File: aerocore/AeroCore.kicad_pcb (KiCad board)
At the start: 2 copper layers, 60 x 60 mm, 50 parts, among them J1 USB_C_Receptacle_USB2.0_16P, J2 Conn_ARM_JTAG_SWD_10, J3 Conn_01x02_Pin, J4 Conn_01x06_Pin, Q1 DMG3418L, U1 RP2040, U2 AP2112K-3.3, U3 MCP73831-2-OT, U4 W25Q16JVUXIQ TR, U5 BMP388, Y2 12MHz

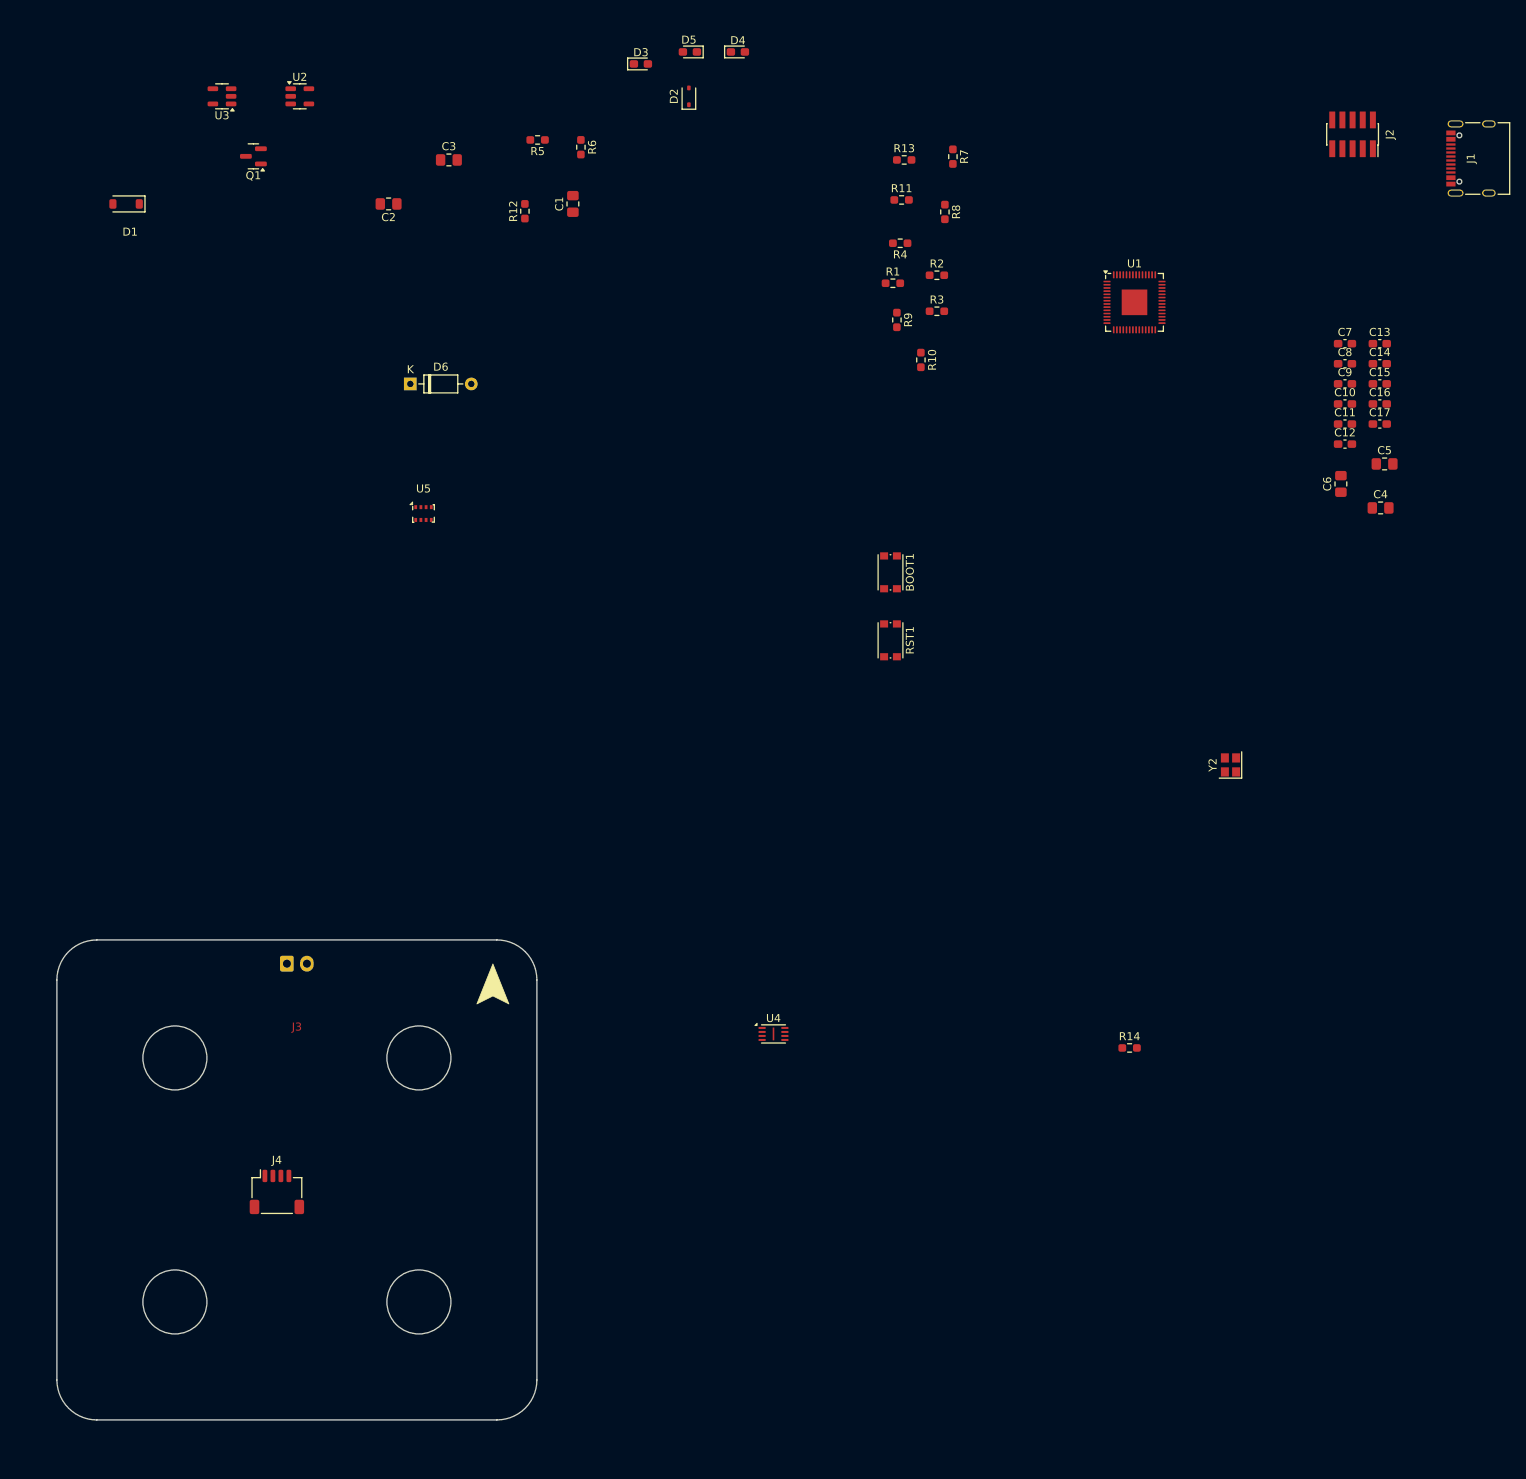
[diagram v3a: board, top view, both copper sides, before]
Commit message: update info for lis3mdltr
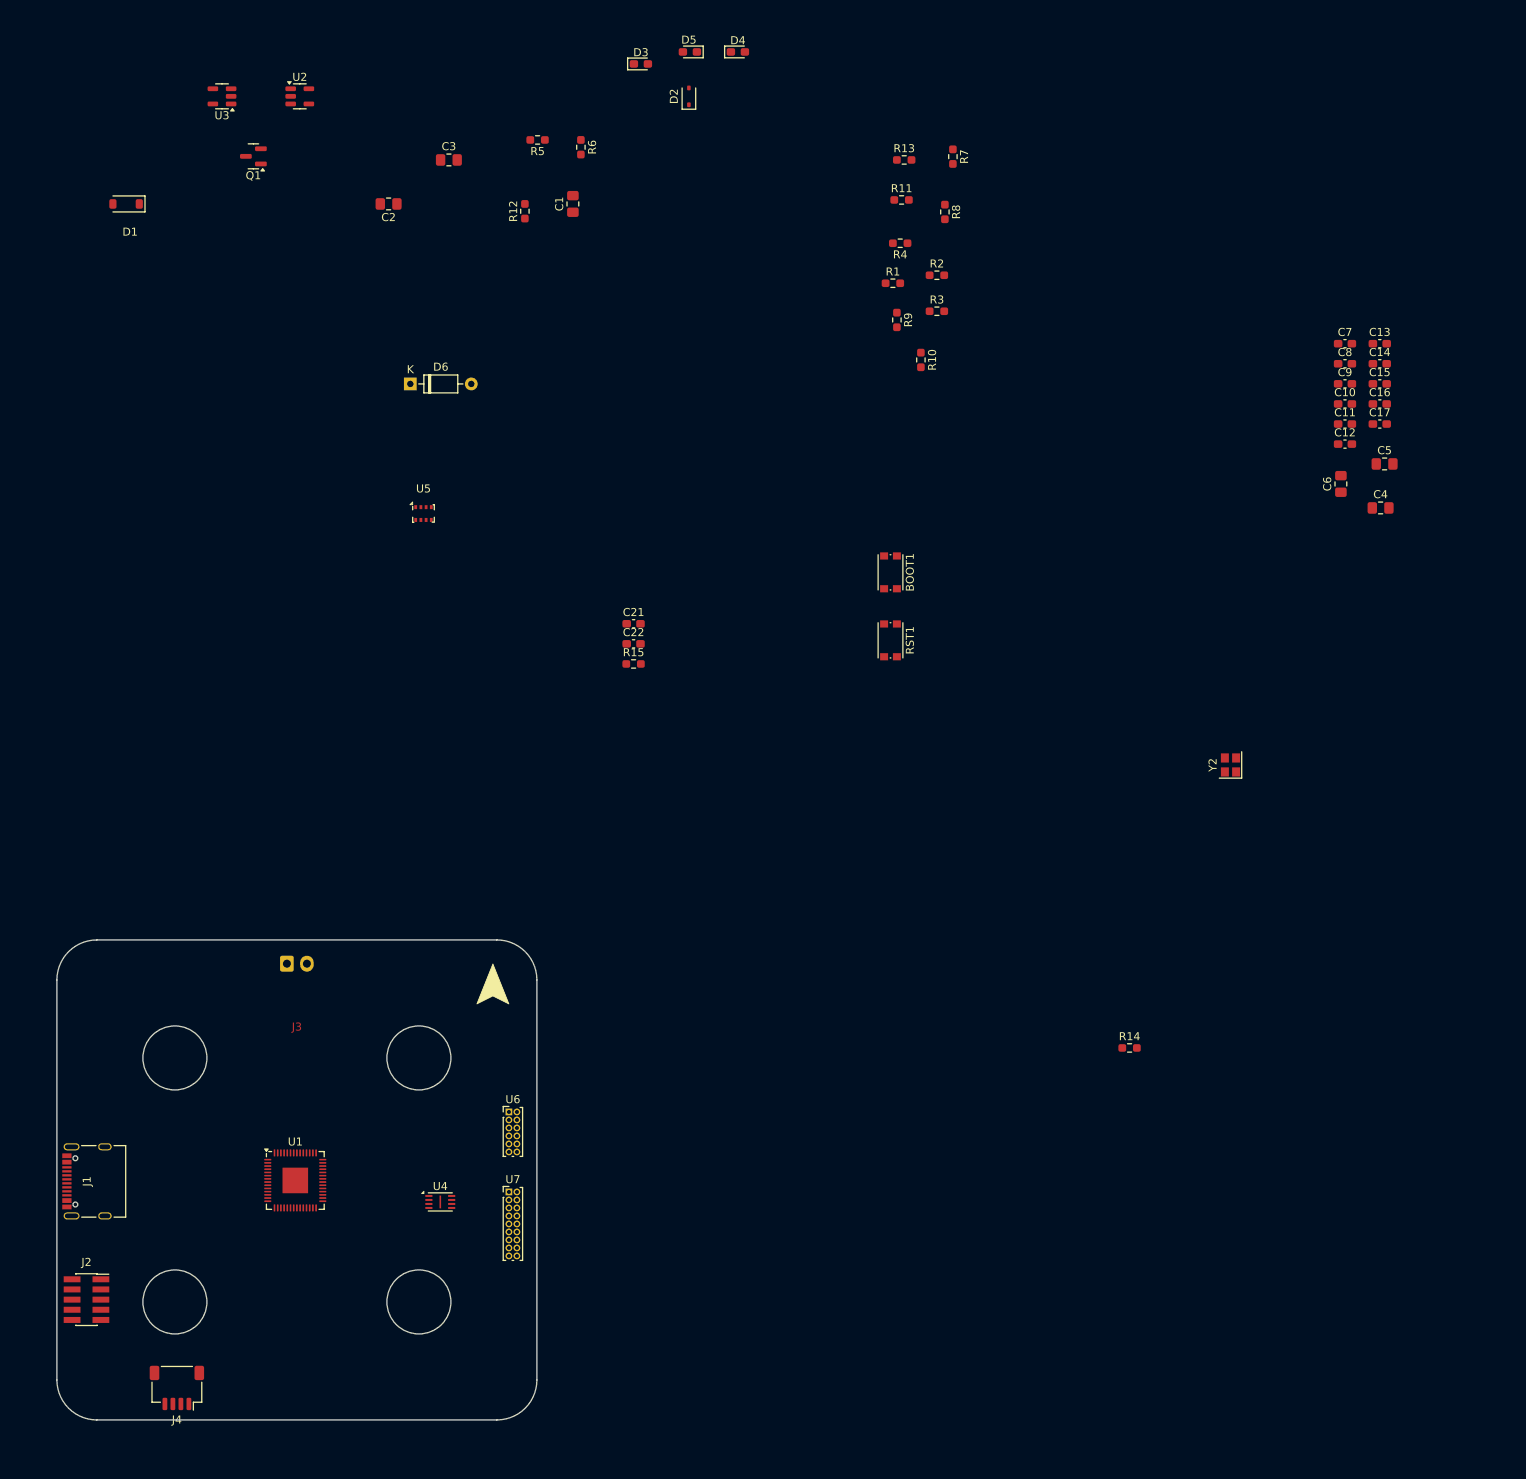
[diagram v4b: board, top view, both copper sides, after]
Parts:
- added C21: 0.1uF, Capacitor_SMD:C_0603_1608Metric_Pad1.08x0.95mm_HandSolder, F.Cu at (92.1, 90.5)
- added C22: 0.1uF, Capacitor_SMD:C_0603_1608Metric_Pad1.08x0.95mm_HandSolder, F.Cu at (92.1, 93.0)
- added R15: 10k, Resistor_SMD:R_0603_1608Metric_Pad0.98x0.95mm_HandSolder, F.Cu at (92.1, 95.5)
- added U6: LIS3MDL, Connector_PinHeader_1.00mm:PinHeader_2x06_P1.00mm_Vertical, F.Cu at (76.5, 151.5)
- added U7: ICM-20649, Connector_PinHeader_1.00mm:PinHeader_2x09_P1.00mm_Vertical, F.Cu at (76.5, 161.5)
- moved J1 215.1 mm to (23.8, 160.2)
- moved J2 215.1 mm to (23.7, 175.0), turned to 0 degrees
- moved U1 151.8 mm to (49.8, 160.1)
- moved U4 46.6 mm to (67.9, 162.8)
- moved J4 27.5 mm to (35.0, 186.0), turned to 180 degrees

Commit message: add pcb for old design
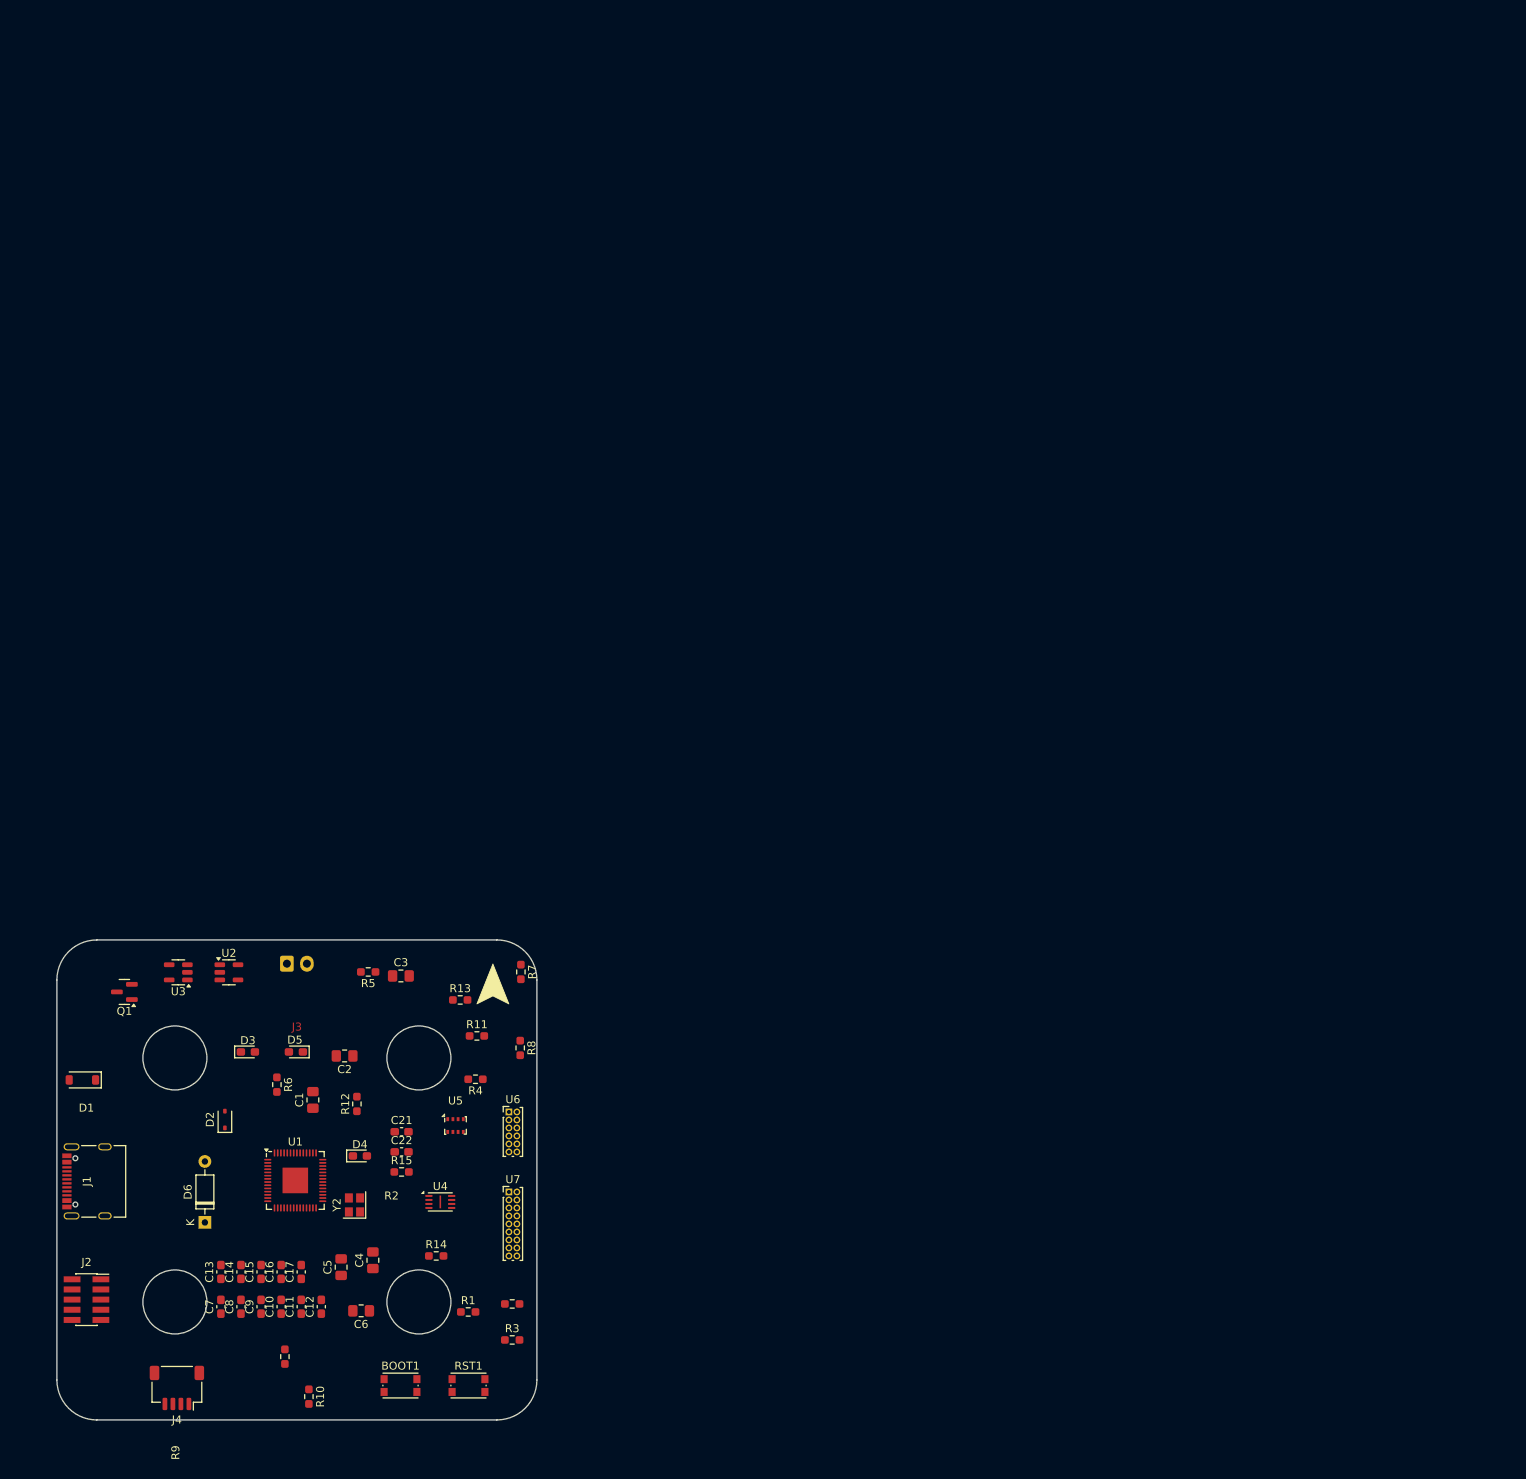
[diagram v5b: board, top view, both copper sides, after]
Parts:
- moved C13 185.6 mm to (40.5, 171.5), turned to 90 degrees
- moved C7 185.0 mm to (40.5, 175.8), turned to 90 degrees
- moved C14 182.1 mm to (43.0, 171.5), turned to 90 degrees
- moved C8 181.5 mm to (43.0, 175.8), turned to 90 degrees
- moved C15 178.5 mm to (45.5, 171.5), turned to 90 degrees
- moved C9 177.9 mm to (45.5, 175.8), turned to 90 degrees
- moved C16 175.0 mm to (48.0, 171.5), turned to 90 degrees
- moved C10 174.4 mm to (48.0, 175.8), turned to 90 degrees
- moved C17 171.5 mm to (50.5, 171.5), turned to 90 degrees
- moved C11 170.9 mm to (50.5, 175.8), turned to 90 degrees
- moved C12 167.3 mm to (53.0, 175.8), turned to 90 degrees
- moved C5 164.6 mm to (55.5, 170.9), turned to 90 degrees
- moved C6 160.3 mm to (58.0, 176.4), turned to 180 degrees
- moved C4 157.2 mm to (59.5, 170.0), turned to 90 degrees
- moved R10 150.5 mm to (51.5, 187.1)
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
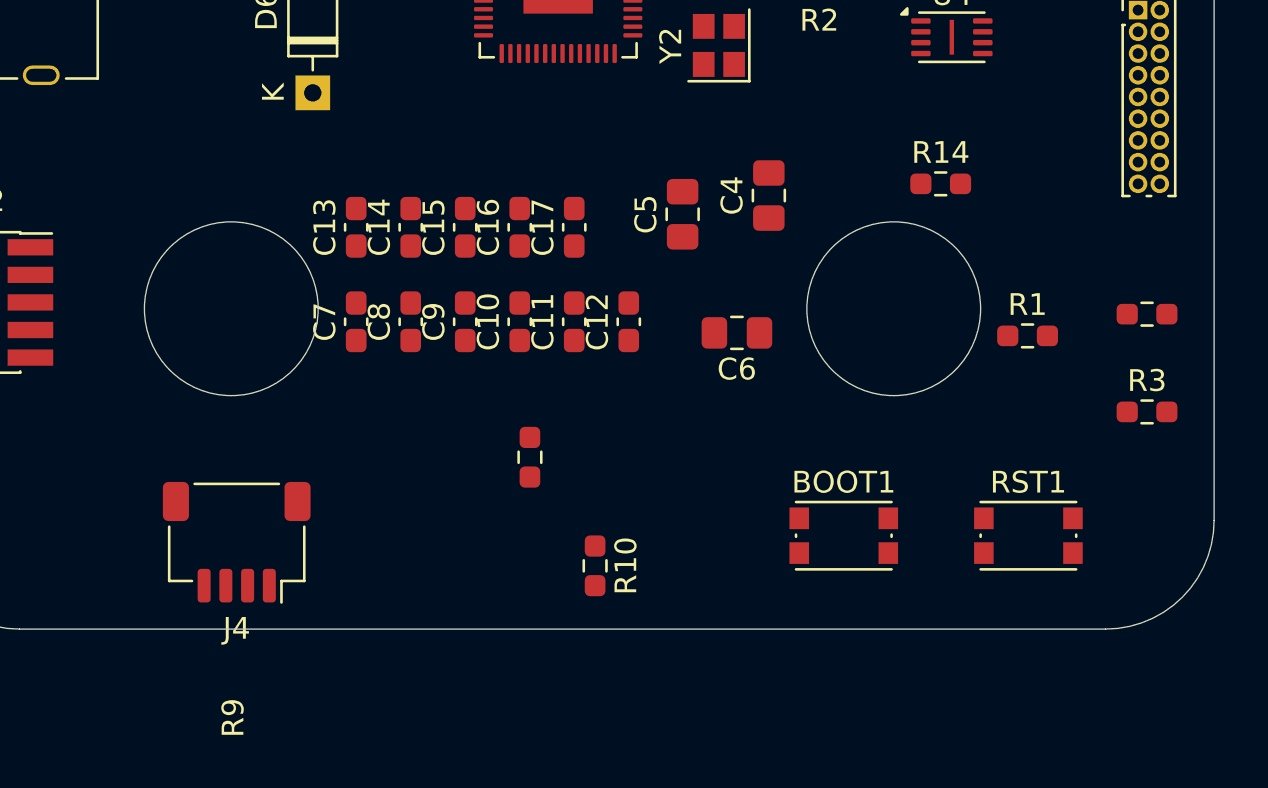
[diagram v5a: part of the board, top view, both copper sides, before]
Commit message: add 3d model on website
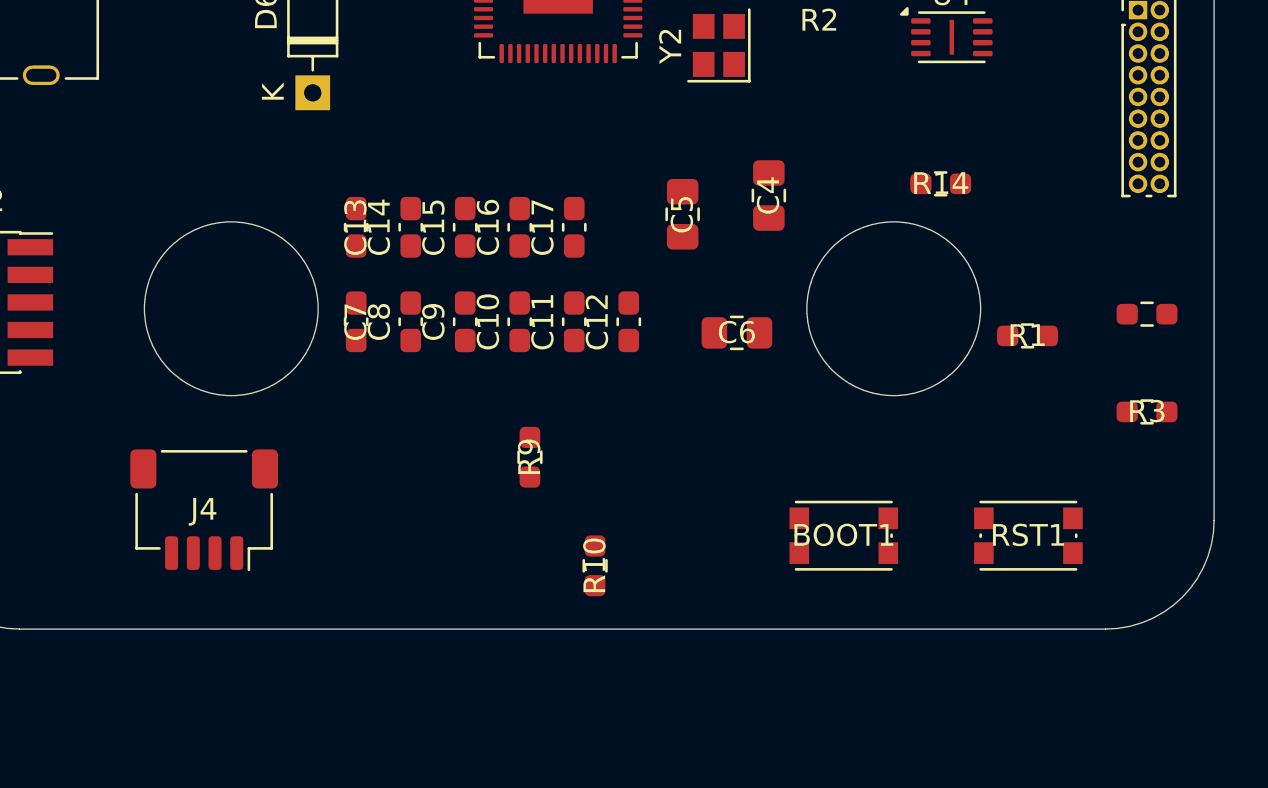
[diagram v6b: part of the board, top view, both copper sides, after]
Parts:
- moved J4 2.12 mm to (33.5, 184.5)
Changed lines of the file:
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@@
 		(tags "capacitor handsolder")
 		(property "Reference" "C13"
-			(at 0 -1.43 90)
+			(at 0 0 90)
 			(layer "F.SilkS")
 			(effects
@@
 		(tags "capacitor handsolder")
 		(property "Reference" "C7"
-			(at 0 -1.43 90)
+			(at 0 0 90)
 			(layer "F.SilkS")
 			(effects
@@
 	(footprint "Connector_JST:JST_SH_SM04B-SRSS-TB_1x04-1MP_P1.00mm_Horizontal"
 		(layer "F.Cu")
-		(at 35 186 180)
+		(at 33.5 184.5 180)
 		(descr "JST SH series connector, SM04B-SRSS-TB (http://www.jst-mfg.com/product/pdf/eng/eSH.pdf), generated with kicad-footprint-generator")
 		(tags "connector JST SH horizontal")
 		(property "Reference" "J4"
-			(at 0 -3.98 360)
+			(at 0 0 360)
 			(layer "F.SilkS")
 			(effects
@@
 		(tags "resistor handsolder")
 		(property "Reference" "R3"
-			(at 0 -1.43 0)
+			(at 0 0 0)
 			(layer "F.SilkS")
 			(effects
@@
 		(tags "tactile switch kmr2")
 		(property "Reference" "BOOT1"
-			(at 0 -2.45 360)
+			(at 0 0 360)
 			(layer "F.SilkS")
 			(effects
@@
 		)
 		(fp_text user "${REFERENCE}"
-			(at 0 -2.45 360)
+			(at 0 0 360)
 			(layer "F.Fab")
 			(effects
@@
 		(tags "resistor handsolder")
 		(property "Reference" "R9"
-			(at 12 13.6575 90)
+			(at 0 0 90)
 			(layer "F.SilkS")
 			(effects
@@
 		(tags "capacitor handsolder")
 		(property "Reference" "C5"
-			(at 0 -1.68 90)
+			(at 0 0 90)
 			(layer "F.SilkS")
 			(effects
@@
 		(tags "capacitor handsolder")
 		(property "Reference" "C4"
-			(at 0 -1.68 90)
+			(at 0 0 90)
 			(layer "F.SilkS")
 			(effects
@@
 		(tags "resistor handsolder")
 		(property "Reference" "R1"
-			(at 0 -1.43 0)
+			(at 0 0 0)
 			(layer "F.SilkS")
 			(effects
@@
 		(tags "capacitor handsolder")
 		(property "Reference" "C6"
-			(at 0 -1.68 360)
+			(at 0 0 360)
 			(layer "F.SilkS")
 			(effects
@@
 		(tags "tactile switch kmr2")
 		(property "Reference" "RST1"
-			(at 0 -2.45 360)
+			(at 0 0 360)
 			(layer "F.SilkS")
 			(effects
@@
 		)
 		(fp_text user "${REFERENCE}"
-			(at 0 -2.45 360)
+			(at 0 0 360)
 			(layer "F.Fab")
 			(effects
@@
 		(tags "resistor handsolder")
 		(property "Reference" "R10"
-			(at 0 -1.43 90)
+			(at 0 0 90)
 			(layer "F.SilkS")
 			(effects
@@
 		(tags "resistor handsolder")
 		(property "Reference" "R14"
-			(at 0 -1.43 0)
+			(at 0 0 0)
 			(layer "F.SilkS")
 			(effects
